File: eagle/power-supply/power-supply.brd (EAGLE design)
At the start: 78.4 x 72.4 mm, 15 parts, among them IC1 7805, IC2 7905, J1 1751251, J2 1751251, Q1 MJL1302A, Q2 MJL3281A

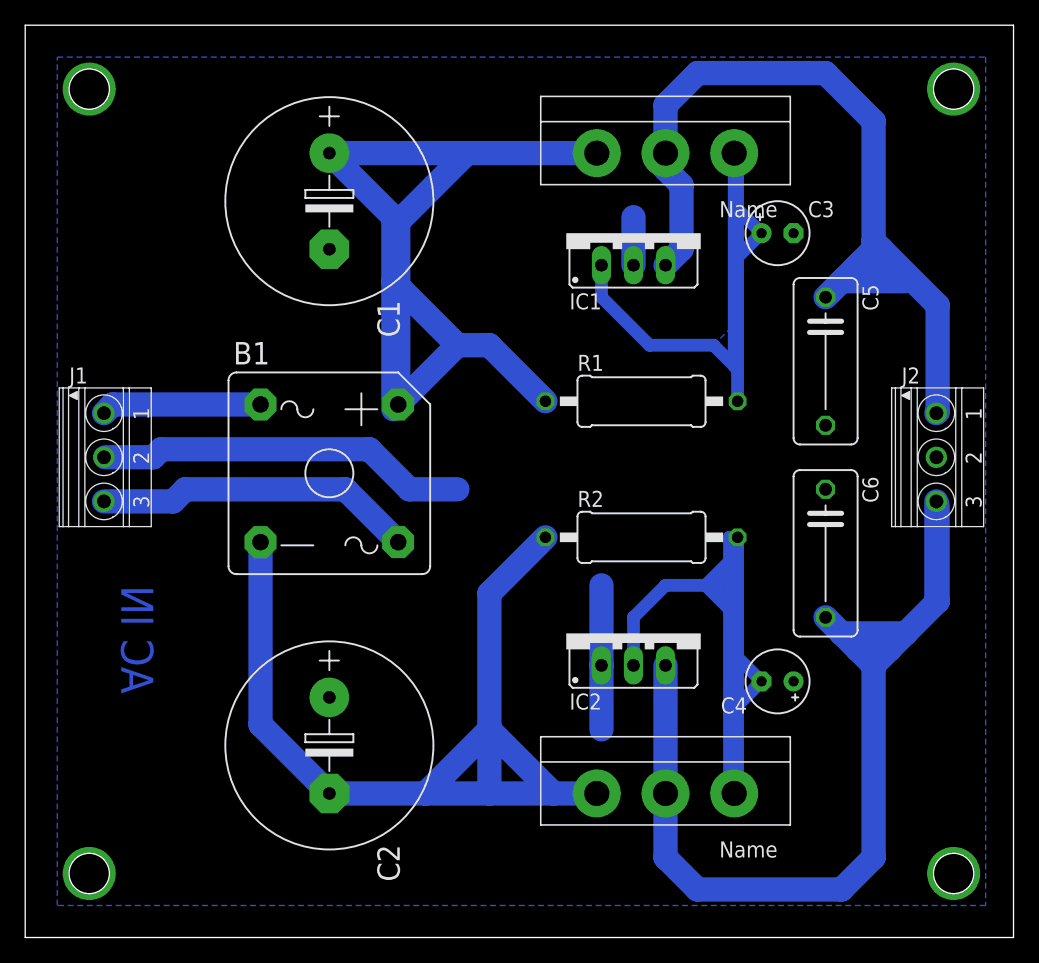
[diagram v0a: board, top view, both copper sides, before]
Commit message: Update power supply board designs to allow heatsinks
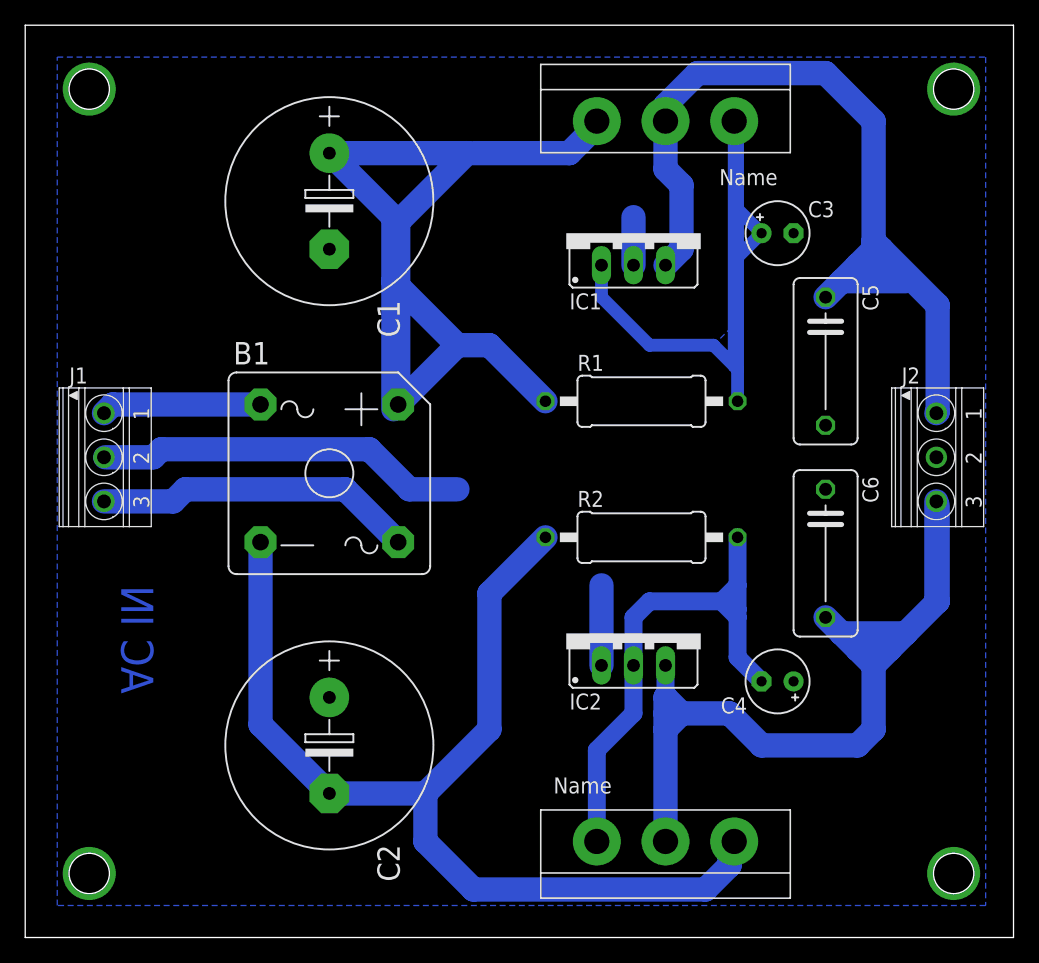
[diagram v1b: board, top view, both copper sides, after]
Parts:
- moved Q2 3.81 mm to (50.8, 7.62), turned to 0 degrees
- moved Q1 2.54 mm to (50.8, 64.8)
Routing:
- net N$7: track 68.1 -> 43.8 mm
- net N$3: track 89.0 -> 101.3 mm
- net N$11: track 84.9 -> 76.5 mm
- net N$8: track 80.0 -> 86.5 mm
- net N$5: track 57.7 -> 62.7 mm
- net GND: track 44.8 -> 39.7 mm
- removed copper zone on layer 16, net N$7
- removed copper zone on layer 16, net N$8

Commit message: Fixes to power supply circuit and board design
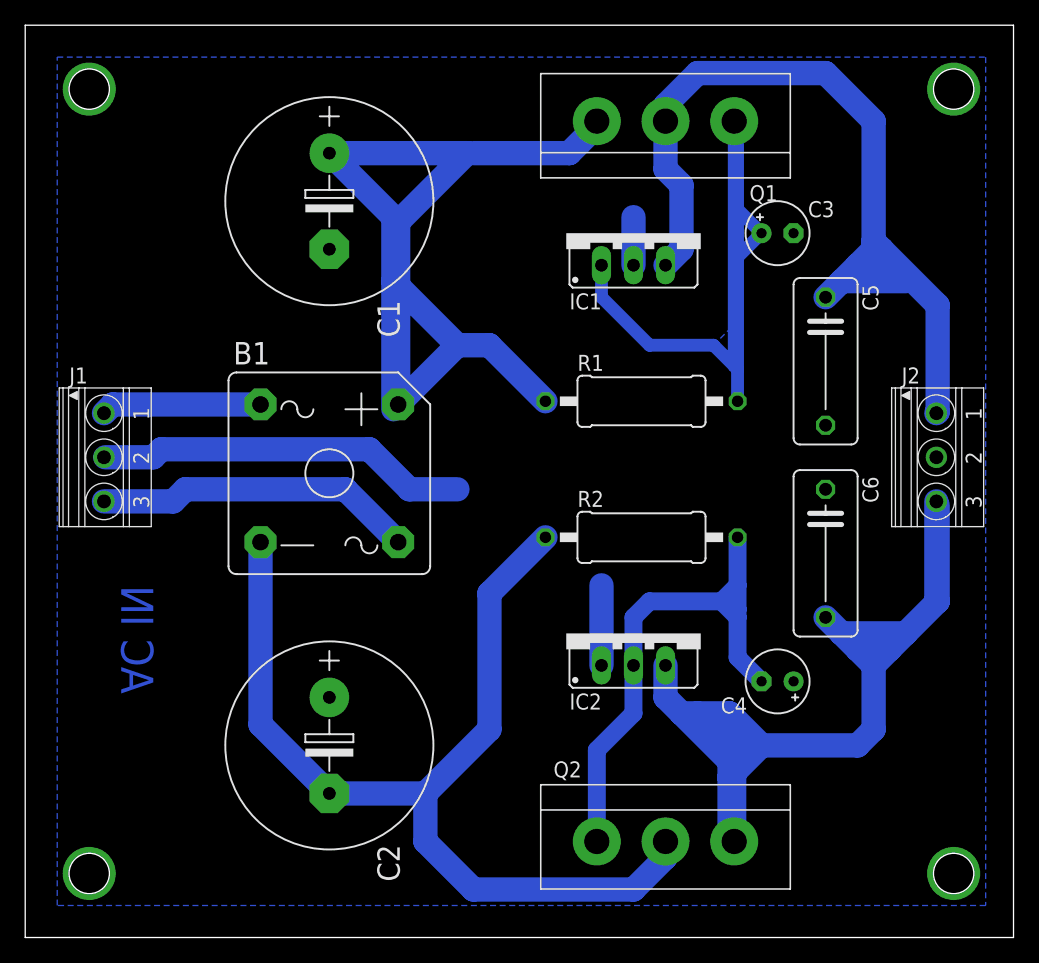
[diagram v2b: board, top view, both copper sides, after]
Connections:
- net N$11: now also Q2.EMITTER; no longer Q2.COLLECTOR
- net N$8: now also Q2.COLLECTOR; no longer Q2.EMITTER
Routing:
- net N$11: track 76.5 -> 92.0 mm
- net N$8: track 86.5 -> 80.8 mm
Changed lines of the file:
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@@
 <signal name="N$11">
 <contactref element="C6" pad="2"/>
-<contactref element="Q2" pad="COLLECTOR"/>
 <contactref element="J2" pad="3"/>
 <contactref element="IC2" pad="OUT"/>
@@
 <wire x1="66.04" y1="22.86" x2="68.58" y2="22.86" width="1.9304" layer="16"/>
 <wire x1="72.39" y1="26.67" x2="72.39" y2="34.29" width="1.9304" layer="16"/>
-<wire x1="50.8" y1="7.62" x2="50.8" y2="16.51" width="1.9304" layer="16"/>
-<wire x1="50.8" y1="16.51" x2="50.8" y2="17.78" width="1.9304" layer="16"/>
-<wire x1="50.8" y1="21.59" x2="50.8" y2="19.05" width="1.4224" layer="16"/>
-<wire x1="50.8" y1="19.05" x2="50.8" y2="17.78" width="1.9304" layer="16"/>
-<wire x1="50.8" y1="17.78" x2="52.07" y2="17.78" width="1.4224" layer="16"/>
-<wire x1="52.07" y1="17.78" x2="55.88" y2="17.78" width="1.9304" layer="16"/>
-<wire x1="55.88" y1="17.78" x2="58.42" y2="15.24" width="1.9304" layer="16"/>
+<wire x1="52.07" y1="17.78" x2="50.8" y2="19.05" width="1.9304" layer="16"/>
+<wire x1="50.8" y1="21.59" x2="50.8" y2="19.05" width="1.9304" layer="16"/>
+<wire x1="52.07" y1="17.78" x2="53.34" y2="17.78" width="1.9304" layer="16"/>
+<wire x1="53.34" y1="17.78" x2="55.88" y2="17.78" width="1.9304" layer="16"/>
 <wire x1="58.42" y1="15.24" x2="66.04" y2="15.24" width="1.9304" layer="16"/>
 <wire x1="66.04" y1="15.24" x2="67.31" y2="16.51" width="1.9304" layer="16"/>
-<wire x1="50.8" y1="16.51" x2="52.07" y2="17.78" width="1.9304" layer="16"/>
-<wire x1="52.07" y1="17.78" x2="50.8" y2="19.05" width="1.9304" layer="16"/>
+<contactref element="Q2" pad="EMITTER"/>
+<wire x1="56.25" y1="7.62" x2="56.25" y2="13.07" width="1.9304" layer="16"/>
+<wire x1="56.25" y1="13.07" x2="58.42" y2="15.24" width="1.9304" layer="16"/>
+<wire x1="55.88" y1="7.62" x2="55.88" y2="12.7" width="1.9304" layer="16"/>
+<wire x1="55.88" y1="13.97" x2="55.88" y2="15.24" width="1.9304" layer="16"/>
+<wire x1="55.88" y1="15.24" x2="55.88" y2="17.78" width="1.9304" layer="16"/>
+<wire x1="55.88" y1="17.78" x2="58.42" y2="15.24" width="1.9304" layer="16"/>
+<wire x1="56.25" y1="13.07" x2="55.88" y2="12.7" width="1.9304" layer="16"/>
+<wire x1="55.88" y1="12.7" x2="55.88" y2="13.97" width="1.9304" layer="16"/>
+<wire x1="55.88" y1="13.97" x2="57.15" y2="15.24" width="1.9304" layer="16"/>
+<wire x1="53.34" y1="17.78" x2="55.88" y2="15.24" width="1.9304" layer="16"/>
+<wire x1="55.88" y1="13.97" x2="52.07" y2="17.78" width="1.9304" layer="16"/>
 </signal>
 <signal name="N$3">
@@
 </signal>
 <signal name="N$8">
-<contactref element="Q2" pad="EMITTER"/>
 <contactref element="R2" pad="1"/>
 <contactref element="C2" pad="-"/>
@@
 <wire x1="31.75" y1="11.43" x2="31.75" y2="7.62" width="1.9304" layer="16"/>
 <wire x1="31.75" y1="7.62" x2="35.56" y2="3.81" width="1.9304" layer="16"/>
-<wire x1="35.56" y1="3.81" x2="53.975" y2="3.81" width="1.9304" layer="16"/>
-<wire x1="53.975" y1="3.81" x2="55.88" y2="5.715" width="1.9304" layer="16"/>
-<wire x1="55.88" y1="5.715" x2="55.88" y2="7.25" width="1.9304" layer="16"/>
-<wire x1="55.88" y1="7.25" x2="56.25" y2="7.62" width="1.9304" layer="16"/>
+<wire x1="35.56" y1="3.81" x2="48.26" y2="3.81" width="1.9304" layer="16"/>
+<contactref element="Q2" pad="COLLECTOR"/>
+<wire x1="50.8" y1="7.62" x2="50.8" y2="6.35" width="1.9304" layer="16"/>
+<wire x1="50.8" y1="6.35" x2="48.26" y2="3.81" width="1.9304" layer="16"/>
 </signal>
 <signal name="N$4">
